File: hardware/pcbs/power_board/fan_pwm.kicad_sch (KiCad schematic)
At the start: 6 parts, among them Q8 IRML6401, U11 4069

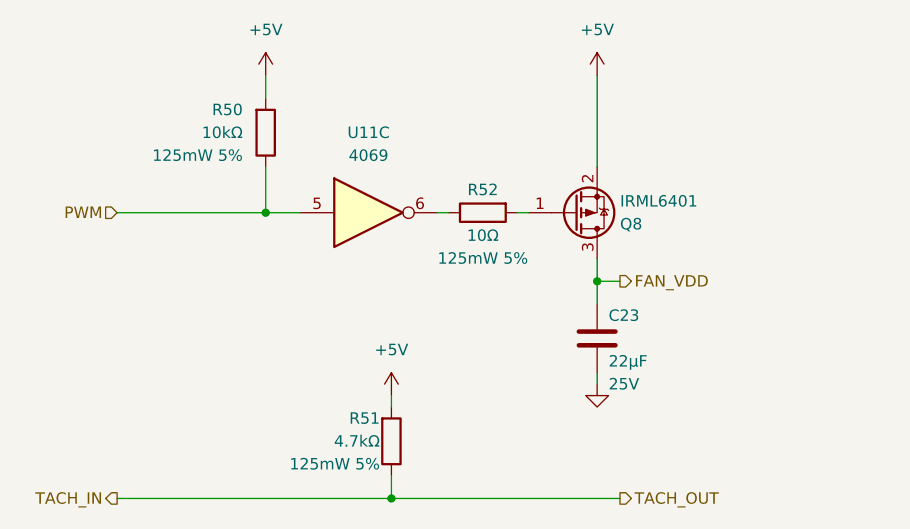
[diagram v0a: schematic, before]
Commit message: power_board: flip 12V connectors
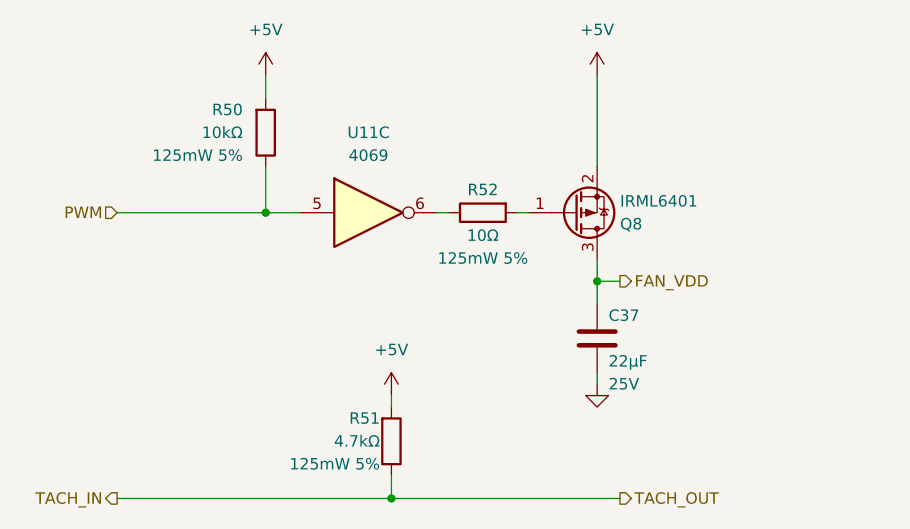
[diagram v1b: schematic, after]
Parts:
- renumbered C23 to C37
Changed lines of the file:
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@@
 		(dnp no)
 		(fields_autoplaced yes)
-		(property "Reference" "#PWR055"
+		(property "Reference" "#PWR0100"
 			(at 168.91 116.84 0)
 			(effects
@@
 		(on_board yes)
 		(dnp no)
-		(property "Reference" "C23"
+		(property "Reference" "C37"
 			(at 170.18 102.87 0)
 			(effects

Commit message: power_board: use USB3-A passthrough connector and fix chg EN
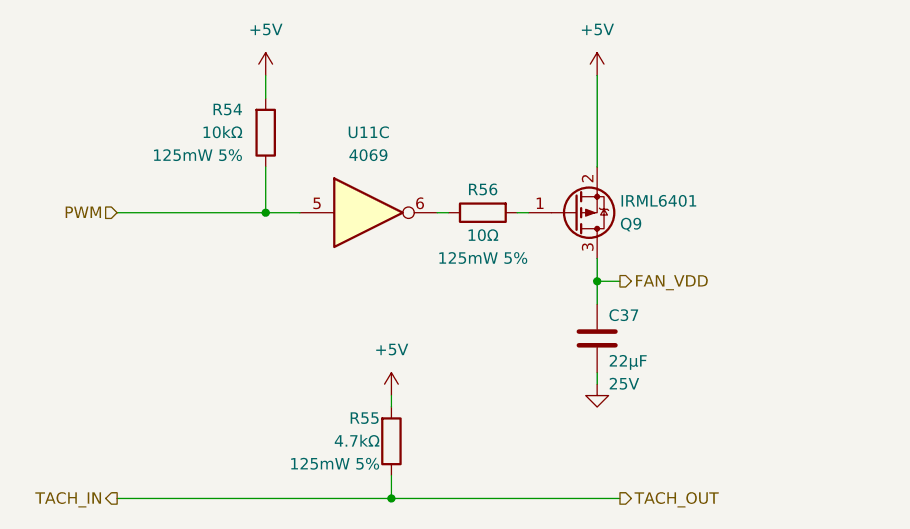
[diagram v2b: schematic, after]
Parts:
- renumbered Q8 to Q9, R50 to R54, R51 to R55, R52 to R56
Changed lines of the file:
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@@
 		(on_board yes)
 		(dnp no)
-		(property "Reference" "R50"
+		(property "Reference" "R54"
 			(at 129.54 80.01 0)
 			(effects
@@
 			(project "power_board"
 				(path "/4b166175-80a4-48c6-994d-6e62a6160b87/f4395b92-97ec-456a-b4c2-238b75f494a2/06607c2e-df57-4ef0-bf70-954d4a07371a"
-					(reference "R50")
+					(reference "R54")
 					(unit 1)
 				)
 				(path "/4b166175-80a4-48c6-994d-6e62a6160b87/f4395b92-97ec-456a-b4c2-238b75f494a2/1f2356c2-5114-44bd-9e00-8022e0f5b6a5"
-					(reference "R29")
+					(reference "R33")
 					(unit 1)
 				)
 				(path "/4b166175-80a4-48c6-994d-6e62a6160b87/f4395b92-97ec-456a-b4c2-238b75f494a2/67d89172-f710-42f2-b66a-20a713f3ef78"
-					(reference "R47")
+					(reference "R51")
 					(unit 1)
 				)
 				(path "/4b166175-80a4-48c6-994d-6e62a6160b87/f4395b92-97ec-456a-b4c2-238b75f494a2/ba1e0391-72e2-478c-ae36-437899b49871"
-					(reference "R32")
+					(reference "R36")
 					(unit 1)
 				)
@@
 		(on_board yes)
 		(dnp no)
-		(property "Reference" "R51"
+		(property "Reference" "R55"
 			(at 144.78 114.3 0)
 			(effects
@@
 			(project "power_board"
 				(path "/4b166175-80a4-48c6-994d-6e62a6160b87/f4395b92-97ec-456a-b4c2-238b75f494a2/06607c2e-df57-4ef0-bf70-954d4a07371a"
-					(reference "R51")
+					(reference "R55")
 					(unit 1)
 				)
 				(path "/4b166175-80a4-48c6-994d-6e62a6160b87/f4395b92-97ec-456a-b4c2-238b75f494a2/1f2356c2-5114-44bd-9e00-8022e0f5b6a5"
-					(reference "R30")
+					(reference "R34")
 					(unit 1)
 				)
 				(path "/4b166175-80a4-48c6-994d-6e62a6160b87/f4395b92-97ec-456a-b4c2-238b75f494a2/67d89172-f710-42f2-b66a-20a713f3ef78"
-					(reference "R48")
+					(reference "R52")
 					(unit 1)
 				)
 				(path "/4b166175-80a4-48c6-994d-6e62a6160b87/f4395b92-97ec-456a-b4c2-238b75f494a2/ba1e0391-72e2-478c-ae36-437899b49871"
-					(reference "R33")
+					(reference "R37")
 					(unit 1)
 				)
@@
 		(on_board yes)
 		(dnp no)
-		(property "Reference" "R52"
+		(property "Reference" "R56"
 			(at 156.21 88.9 90)
 			(effects
@@
 			(project "power_board"
 				(path "/4b166175-80a4-48c6-994d-6e62a6160b87/f4395b92-97ec-456a-b4c2-238b75f494a2/06607c2e-df57-4ef0-bf70-954d4a07371a"
-					(reference "R52")
+					(reference "R56")
 					(unit 1)
 				)
 				(path "/4b166175-80a4-48c6-994d-6e62a6160b87/f4395b92-97ec-456a-b4c2-238b75f494a2/1f2356c2-5114-44bd-9e00-8022e0f5b6a5"
-					(reference "R31")
+					(reference "R35")
 					(unit 1)
 				)
 				(path "/4b166175-80a4-48c6-994d-6e62a6160b87/f4395b92-97ec-456a-b4c2-238b75f494a2/67d89172-f710-42f2-b66a-20a713f3ef78"
-					(reference "R49")
+					(reference "R53")
 					(unit 1)
 				)
 				(path "/4b166175-80a4-48c6-994d-6e62a6160b87/f4395b92-97ec-456a-b4c2-238b75f494a2/ba1e0391-72e2-478c-ae36-437899b49871"
-					(reference "R34")
+					(reference "R38")
 					(unit 1)
 				)
@@
 		(on_board yes)
 		(dnp no)
-		(property "Reference" "Q8"
+		(property "Reference" "Q9"
 			(at 171.45 92.71 0)
 			(effects
@@
 			(project "power_board"
 				(path "/4b166175-80a4-48c6-994d-6e62a6160b87/f4395b92-97ec-456a-b4c2-238b75f494a2/06607c2e-df57-4ef0-bf70-954d4a07371a"
+					(reference "Q9")
+					(unit 1)
+				)
+				(path "/4b166175-80a4-48c6-994d-6e62a6160b87/f4395b92-97ec-456a-b4c2-238b75f494a2/1f2356c2-5114-44bd-9e00-8022e0f5b6a5"
+					(reference "Q3")
+					(unit 1)
+				)
+				(path "/4b166175-80a4-48c6-994d-6e62a6160b87/f4395b92-97ec-456a-b4c2-238b75f494a2/67d89172-f710-42f2-b66a-20a713f3ef78"
 					(reference "Q8")
 					(unit 1)
 				)
-				(path "/4b166175-80a4-48c6-994d-6e62a6160b87/f4395b92-97ec-456a-b4c2-238b75f494a2/1f2356c2-5114-44bd-9e00-8022e0f5b6a5"
-					(reference "Q2")
-					(unit 1)
-				)
-				(path "/4b166175-80a4-48c6-994d-6e62a6160b87/f4395b92-97ec-456a-b4c2-238b75f494a2/67d89172-f710-42f2-b66a-20a713f3ef78"
-					(reference "Q7")
-					(unit 1)
-				)
 				(path "/4b166175-80a4-48c6-994d-6e62a6160b87/f4395b92-97ec-456a-b4c2-238b75f494a2/ba1e0391-72e2-478c-ae36-437899b49871"
-					(reference "Q3")
-					(unit 1)
-				)
+					(reference "Q4")
+					(unit 1)
+				)

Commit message: power_board: add protection resistor to overload signal
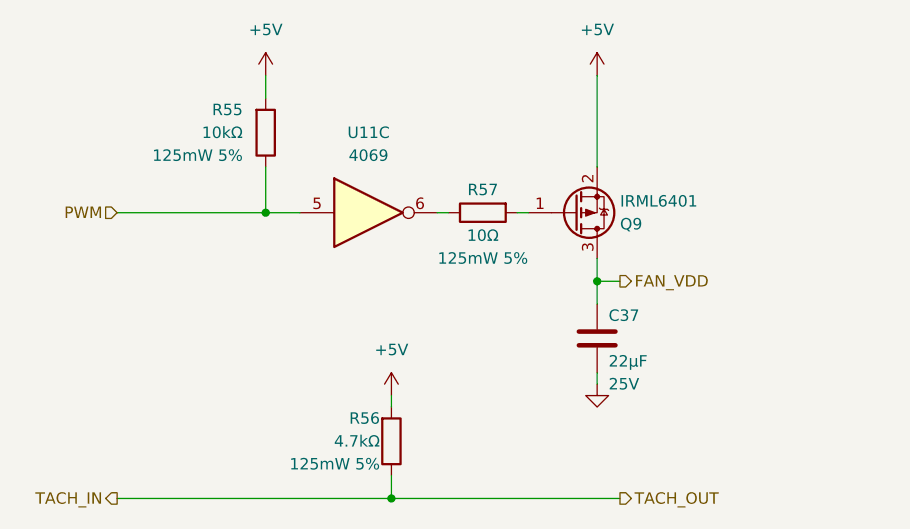
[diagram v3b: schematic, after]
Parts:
- renumbered R54 to R55, R55 to R56, R56 to R57
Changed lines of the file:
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@@
 		(on_board yes)
 		(dnp no)
-		(property "Reference" "R54"
+		(property "Reference" "R55"
 			(at 129.54 80.01 0)
 			(effects
@@
 			(project "power_board"
 				(path "/4b166175-80a4-48c6-994d-6e62a6160b87/f4395b92-97ec-456a-b4c2-238b75f494a2/06607c2e-df57-4ef0-bf70-954d4a07371a"
-					(reference "R54")
+					(reference "R55")
 					(unit 1)
 				)
 				(path "/4b166175-80a4-48c6-994d-6e62a6160b87/f4395b92-97ec-456a-b4c2-238b75f494a2/1f2356c2-5114-44bd-9e00-8022e0f5b6a5"
-					(reference "R33")
+					(reference "R34")
 					(unit 1)
 				)
 				(path "/4b166175-80a4-48c6-994d-6e62a6160b87/f4395b92-97ec-456a-b4c2-238b75f494a2/67d89172-f710-42f2-b66a-20a713f3ef78"
-					(reference "R51")
+					(reference "R52")
 					(unit 1)
 				)
 				(path "/4b166175-80a4-48c6-994d-6e62a6160b87/f4395b92-97ec-456a-b4c2-238b75f494a2/ba1e0391-72e2-478c-ae36-437899b49871"
-					(reference "R36")
+					(reference "R37")
 					(unit 1)
 				)
@@
 		(on_board yes)
 		(dnp no)
-		(property "Reference" "R55"
+		(property "Reference" "R56"
 			(at 144.78 114.3 0)
 			(effects
@@
 			(project "power_board"
 				(path "/4b166175-80a4-48c6-994d-6e62a6160b87/f4395b92-97ec-456a-b4c2-238b75f494a2/06607c2e-df57-4ef0-bf70-954d4a07371a"
-					(reference "R55")
+					(reference "R56")
 					(unit 1)
 				)
 				(path "/4b166175-80a4-48c6-994d-6e62a6160b87/f4395b92-97ec-456a-b4c2-238b75f494a2/1f2356c2-5114-44bd-9e00-8022e0f5b6a5"
-					(reference "R34")
+					(reference "R35")
 					(unit 1)
 				)
 				(path "/4b166175-80a4-48c6-994d-6e62a6160b87/f4395b92-97ec-456a-b4c2-238b75f494a2/67d89172-f710-42f2-b66a-20a713f3ef78"
-					(reference "R52")
+					(reference "R53")
 					(unit 1)
 				)
 				(path "/4b166175-80a4-48c6-994d-6e62a6160b87/f4395b92-97ec-456a-b4c2-238b75f494a2/ba1e0391-72e2-478c-ae36-437899b49871"
-					(reference "R37")
+					(reference "R38")
 					(unit 1)
 				)
@@
 		(on_board yes)
 		(dnp no)
-		(property "Reference" "R56"
+		(property "Reference" "R57"
 			(at 156.21 88.9 90)
 			(effects
@@
 			(project "power_board"
 				(path "/4b166175-80a4-48c6-994d-6e62a6160b87/f4395b92-97ec-456a-b4c2-238b75f494a2/06607c2e-df57-4ef0-bf70-954d4a07371a"
-					(reference "R56")
+					(reference "R57")
 					(unit 1)
 				)
 				(path "/4b166175-80a4-48c6-994d-6e62a6160b87/f4395b92-97ec-456a-b4c2-238b75f494a2/1f2356c2-5114-44bd-9e00-8022e0f5b6a5"
-					(reference "R35")
+					(reference "R36")
 					(unit 1)
 				)
 				(path "/4b166175-80a4-48c6-994d-6e62a6160b87/f4395b92-97ec-456a-b4c2-238b75f494a2/67d89172-f710-42f2-b66a-20a713f3ef78"
-					(reference "R53")
+					(reference "R54")
 					(unit 1)
 				)
 				(path "/4b166175-80a4-48c6-994d-6e62a6160b87/f4395b92-97ec-456a-b4c2-238b75f494a2/ba1e0391-72e2-478c-ae36-437899b49871"
-					(reference "R38")
-					(unit 1)
-				)
+					(reference "R39")
+					(unit 1)
+				)

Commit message: power_board: proper enable circuit for meanwell power modules
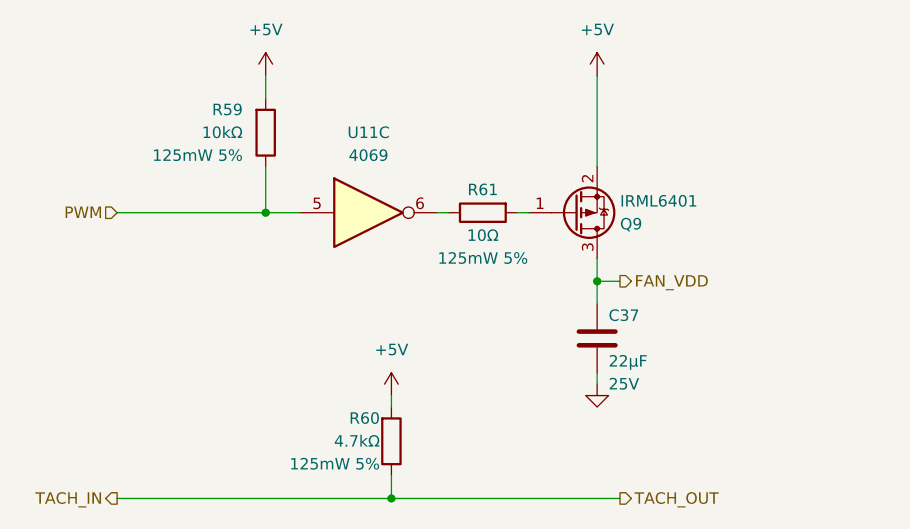
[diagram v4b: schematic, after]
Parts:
- renumbered R55 to R59, R56 to R60, R57 to R61
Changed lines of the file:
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@@
 		(on_board yes)
 		(dnp no)
-		(property "Reference" "R55"
+		(property "Reference" "R59"
 			(at 129.54 80.01 0)
 			(effects
@@
 			(project "power_board"
 				(path "/4b166175-80a4-48c6-994d-6e62a6160b87/f4395b92-97ec-456a-b4c2-238b75f494a2/06607c2e-df57-4ef0-bf70-954d4a07371a"
-					(reference "R55")
+					(reference "R59")
 					(unit 1)
 				)
 				(path "/4b166175-80a4-48c6-994d-6e62a6160b87/f4395b92-97ec-456a-b4c2-238b75f494a2/1f2356c2-5114-44bd-9e00-8022e0f5b6a5"
-					(reference "R34")
+					(reference "R38")
 					(unit 1)
 				)
 				(path "/4b166175-80a4-48c6-994d-6e62a6160b87/f4395b92-97ec-456a-b4c2-238b75f494a2/67d89172-f710-42f2-b66a-20a713f3ef78"
-					(reference "R52")
+					(reference "R56")
 					(unit 1)
 				)
 				(path "/4b166175-80a4-48c6-994d-6e62a6160b87/f4395b92-97ec-456a-b4c2-238b75f494a2/ba1e0391-72e2-478c-ae36-437899b49871"
-					(reference "R37")
+					(reference "R41")
 					(unit 1)
 				)
@@
 		(on_board yes)
 		(dnp no)
-		(property "Reference" "R56"
+		(property "Reference" "R60"
 			(at 144.78 114.3 0)
 			(effects
@@
 			(project "power_board"
 				(path "/4b166175-80a4-48c6-994d-6e62a6160b87/f4395b92-97ec-456a-b4c2-238b75f494a2/06607c2e-df57-4ef0-bf70-954d4a07371a"
-					(reference "R56")
+					(reference "R60")
 					(unit 1)
 				)
 				(path "/4b166175-80a4-48c6-994d-6e62a6160b87/f4395b92-97ec-456a-b4c2-238b75f494a2/1f2356c2-5114-44bd-9e00-8022e0f5b6a5"
-					(reference "R35")
+					(reference "R39")
 					(unit 1)
 				)
 				(path "/4b166175-80a4-48c6-994d-6e62a6160b87/f4395b92-97ec-456a-b4c2-238b75f494a2/67d89172-f710-42f2-b66a-20a713f3ef78"
-					(reference "R53")
+					(reference "R57")
 					(unit 1)
 				)
 				(path "/4b166175-80a4-48c6-994d-6e62a6160b87/f4395b92-97ec-456a-b4c2-238b75f494a2/ba1e0391-72e2-478c-ae36-437899b49871"
-					(reference "R38")
+					(reference "R42")
 					(unit 1)
 				)
@@
 		(on_board yes)
 		(dnp no)
-		(property "Reference" "R57"
+		(property "Reference" "R61"
 			(at 156.21 88.9 90)
 			(effects
@@
 			(project "power_board"
 				(path "/4b166175-80a4-48c6-994d-6e62a6160b87/f4395b92-97ec-456a-b4c2-238b75f494a2/06607c2e-df57-4ef0-bf70-954d4a07371a"
-					(reference "R57")
+					(reference "R61")
 					(unit 1)
 				)
 				(path "/4b166175-80a4-48c6-994d-6e62a6160b87/f4395b92-97ec-456a-b4c2-238b75f494a2/1f2356c2-5114-44bd-9e00-8022e0f5b6a5"
-					(reference "R36")
+					(reference "R40")
 					(unit 1)
 				)
 				(path "/4b166175-80a4-48c6-994d-6e62a6160b87/f4395b92-97ec-456a-b4c2-238b75f494a2/67d89172-f710-42f2-b66a-20a713f3ef78"
-					(reference "R54")
+					(reference "R58")
 					(unit 1)
 				)
 				(path "/4b166175-80a4-48c6-994d-6e62a6160b87/f4395b92-97ec-456a-b4c2-238b75f494a2/ba1e0391-72e2-478c-ae36-437899b49871"
-					(reference "R39")
-					(unit 1)
-				)
+					(reference "R43")
+					(unit 1)
+				)

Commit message: power_board: axe one fan output to make space for caps
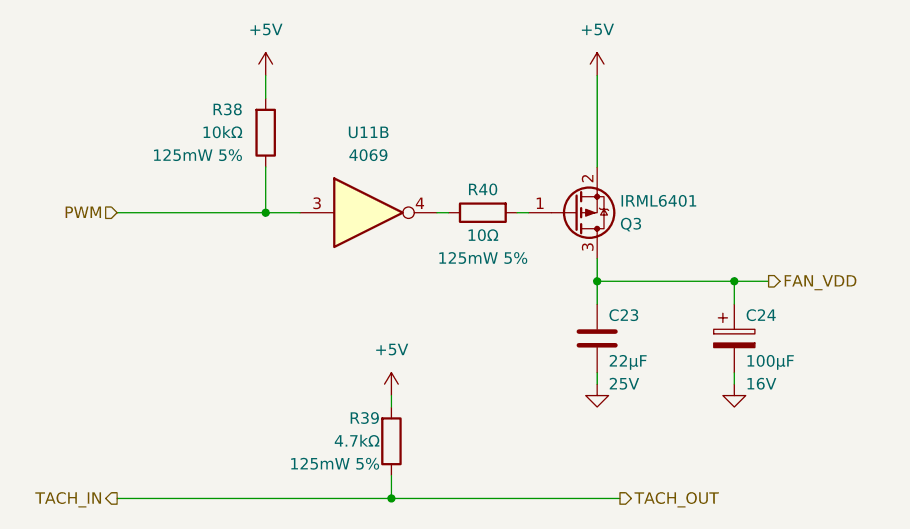
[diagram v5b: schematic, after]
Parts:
- added C24: 100μF, Capacitor_THT:CP_Radial_D5.0mm_P2.00mm, symbol Device:C_Polarized
- renumbered C37 to C23, Q9 to Q3, R59 to R38, R60 to R39, R61 to R40
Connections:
- net FAN_VDD: now also C24.1
- net GND: now also C24.2
- net PWM: now also U11.3; no longer U11.5
- net at R40.1: now also U11.4; no longer U11.6

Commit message: power_board: THERE ARE FOUR FANS
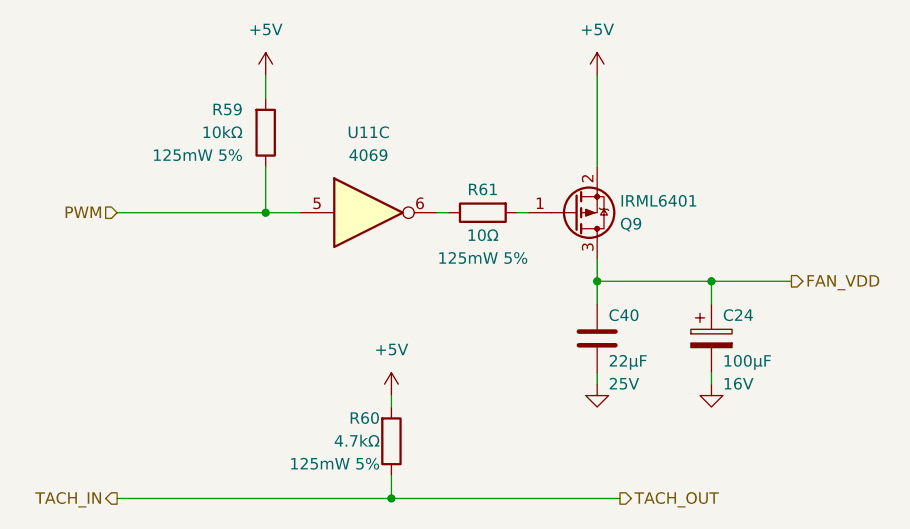
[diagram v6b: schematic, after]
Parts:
- renumbered C23 to C40, Q3 to Q9, R38 to R59, R39 to R60, R40 to R61
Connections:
- net PWM: now also U11.5; no longer U11.3
- net at R61.1: now also U11.6; no longer U11.4

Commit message: power_board: use another isolated power module
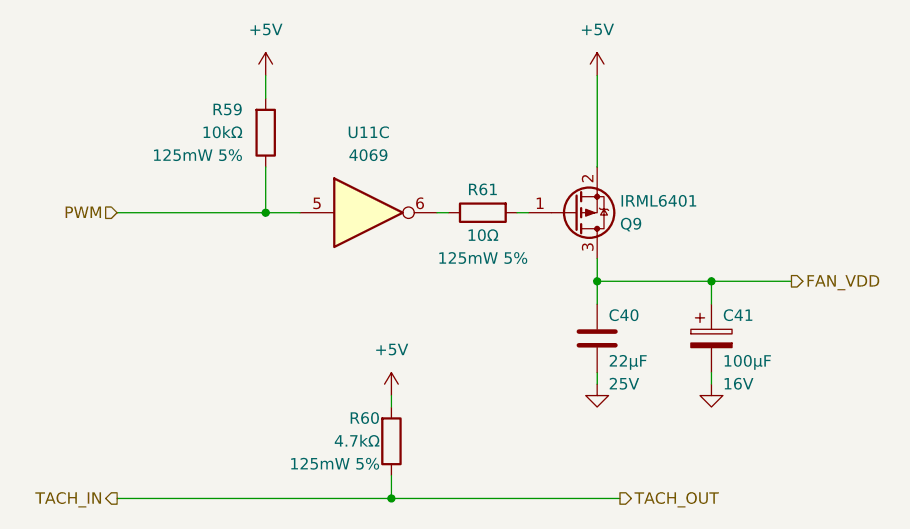
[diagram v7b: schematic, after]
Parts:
- renumbered C24 to C41
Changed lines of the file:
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@@
 		(on_board yes)
 		(dnp no)
-		(property "Reference" "C24"
+		(property "Reference" "C41"
 			(at 182.88 102.87 0)
 			(effects
@@
 		(dnp no)
 		(fields_autoplaced yes)
-		(property "Reference" "#PWR056"
+		(property "Reference" "#PWR0104"
 			(at 181.61 116.84 0)
 			(effects
